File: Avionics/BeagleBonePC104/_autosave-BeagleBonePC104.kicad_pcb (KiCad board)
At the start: 2 copper layers, 90.2 x 95.9 mm, 17 parts, among them U4 TJA1051T-3, U5 TMP36xS

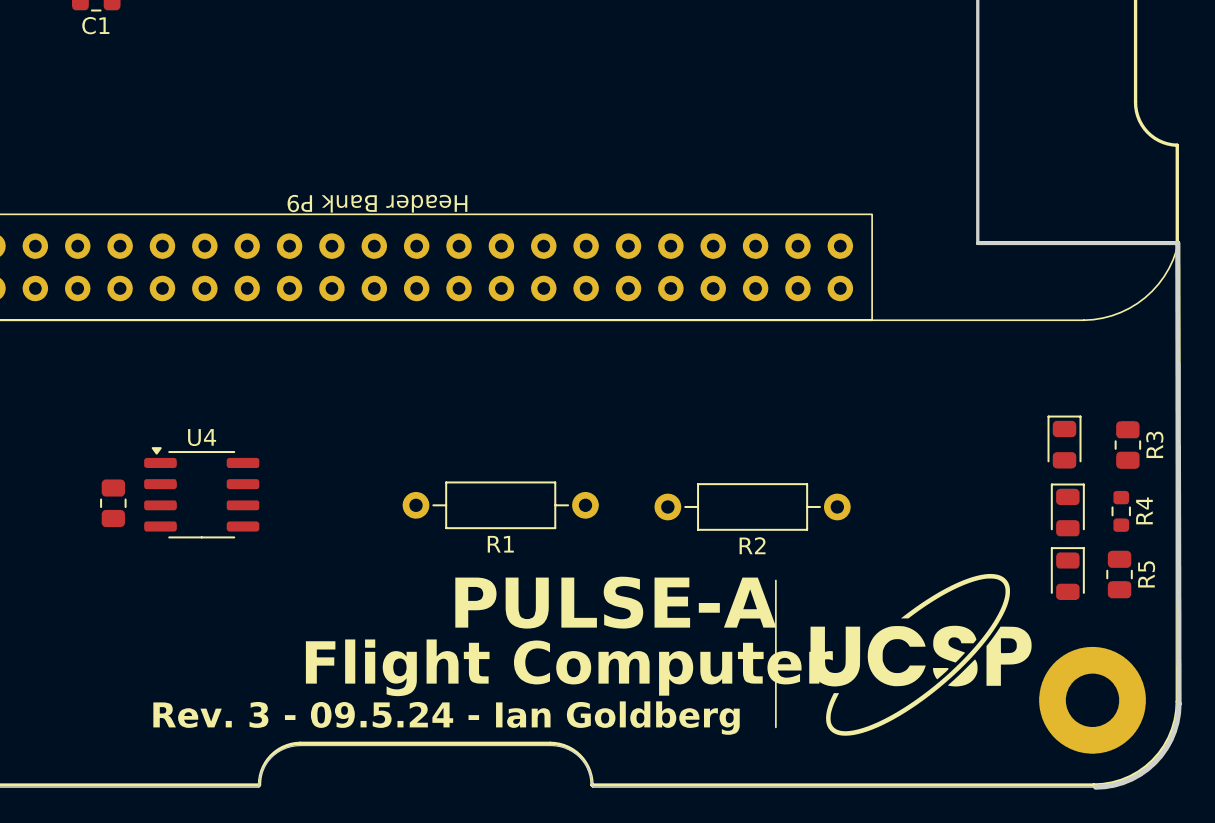
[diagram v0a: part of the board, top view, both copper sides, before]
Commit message: Ian Goldberg - Made changes to the third revision of the flight computer board, trying to figure out a way to power it throught ht header connector while still extracting data (through ethernet).
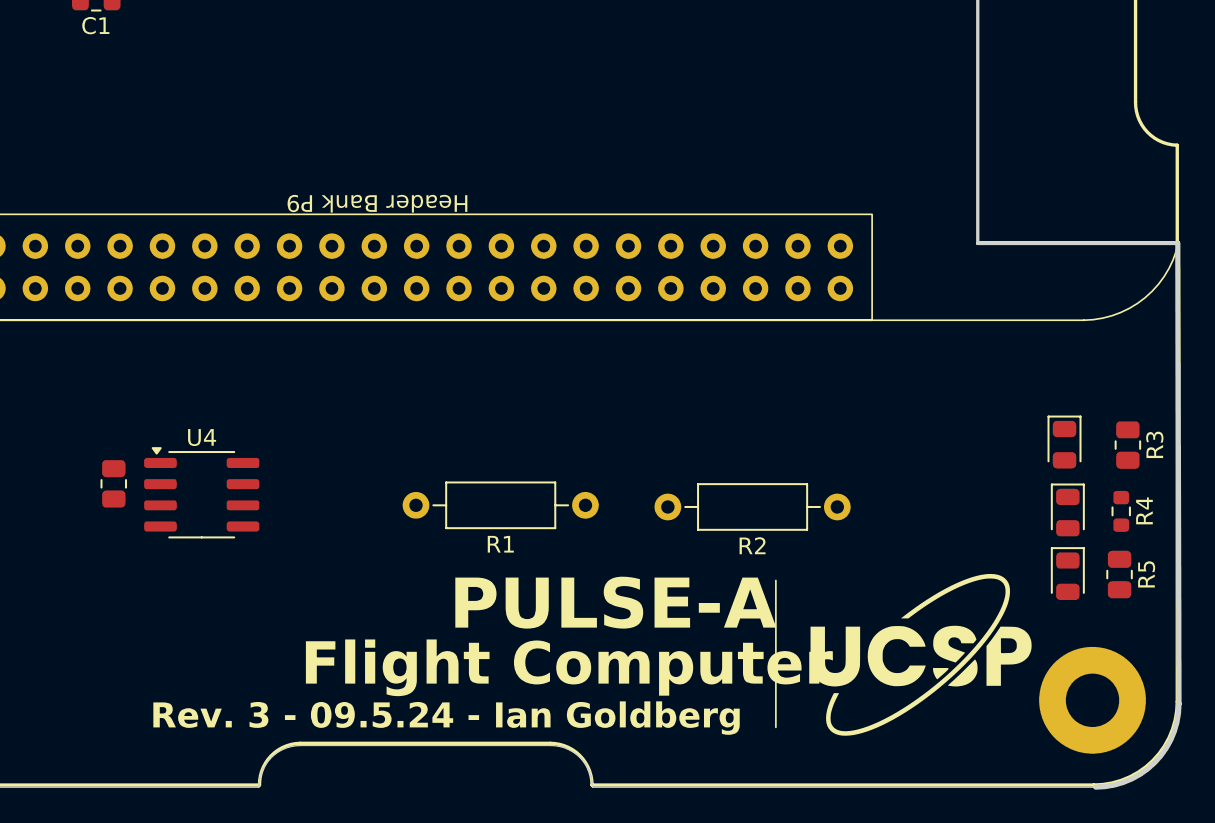
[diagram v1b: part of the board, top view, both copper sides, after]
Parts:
- moved R6 1.17 mm to (106.3, 151.8)
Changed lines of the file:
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@@
 		(fp_arc
 			(start 35.147914 0)
-			(mid 35.848689 -1.754737)
+			(mid 35.848689 -1.75474)
 			(end 37.585 -2.5)
 			(stroke
@@
 		(fp_arc
 			(start 90.17 -38.358018)
-			(mid 88.379929 -39.143694)
+			(mid 88.379902 -39.143666)
 			(end 87.67 -40.965104)
 			(stroke
@@
 	(footprint "Resistor_SMD:R_0805_2012Metric"
 		(layer "F.Cu")
-		(at 106.275 152.9775 90)
+		(at 106.3 151.8125 90)
 		(descr "Resistor SMD 0805 (2012 Metric), square (rectangular) end terminal, IPC_7351 nominal, (Body size source: IPC-SM-782 page 72, https://www.pcb-3d.com/wordpress/wp-content/uploads/ipc-sm-782a_amendment_1_and_2.pdf), generated with kicad-footprint-generator")
 		(tags "resistor")
